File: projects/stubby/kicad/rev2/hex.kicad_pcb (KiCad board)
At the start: 2 copper layers, 49.5 x 49.5 mm, 62 parts, among them IC1 ATMEGA1284-A, P1 CONN_6, P10 PROG, P11 CONN_6, P2 CONN_6, P3 CONN_10, P4 CONN_13, P5 CONN_4, P6 CONN_2, P7 CONN_1, P8 CONN_4, P9 BATT (4.8V-6V), SW1 DPDT, X1 CRYSTAL_RESONATOR

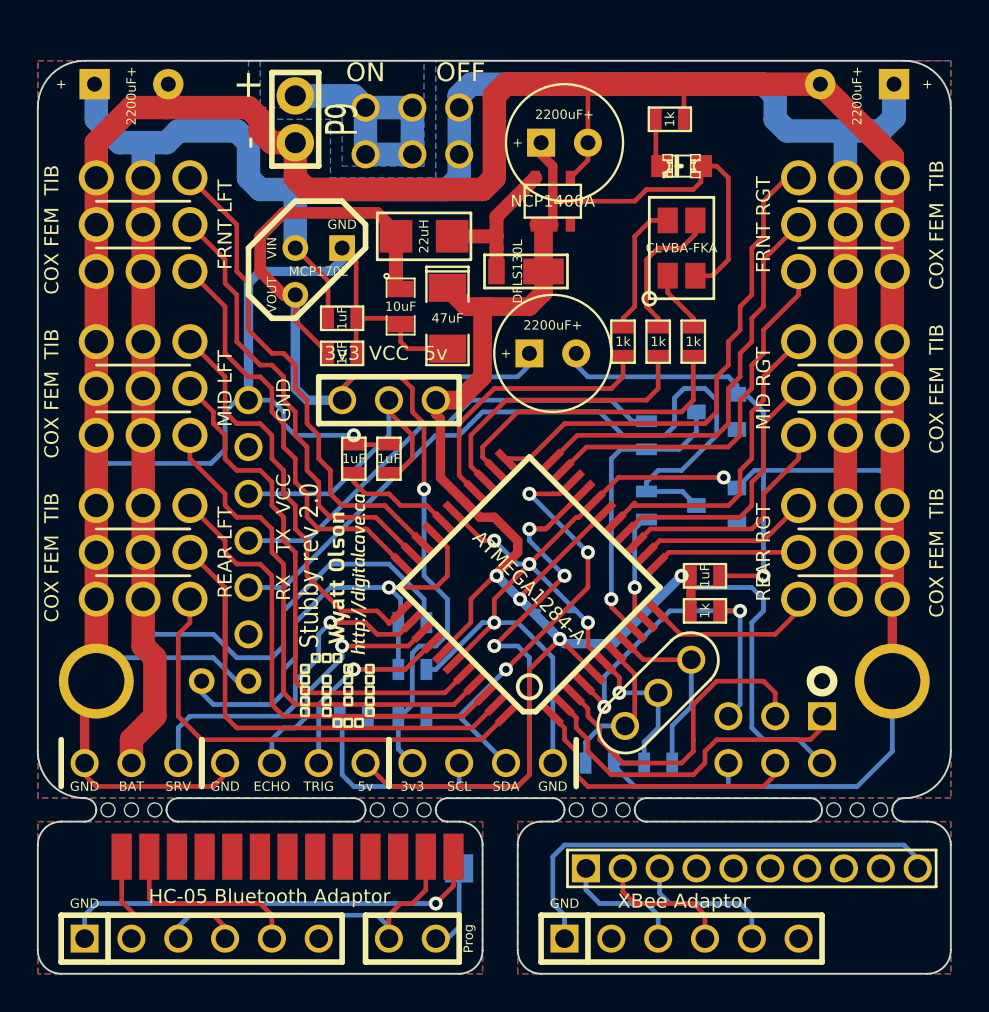
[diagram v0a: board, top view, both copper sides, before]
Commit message: A bit of trace cleanup
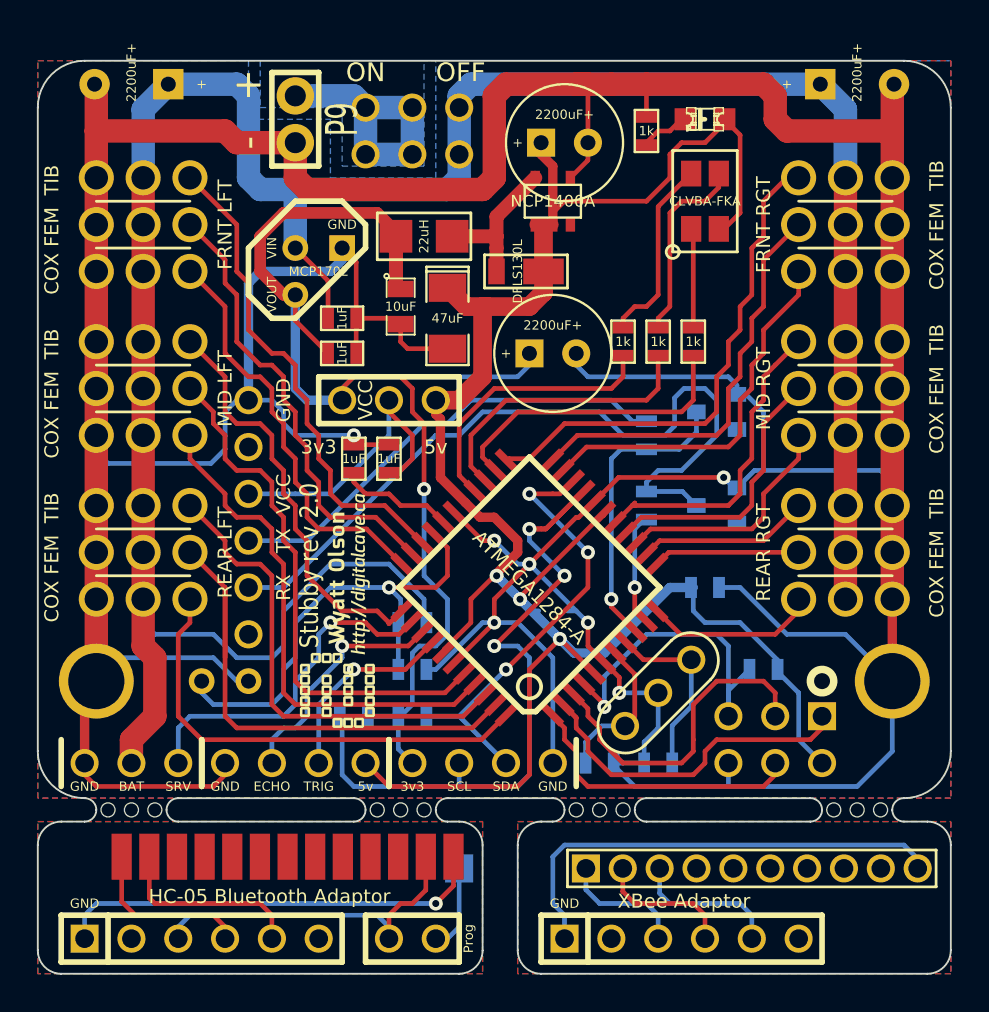
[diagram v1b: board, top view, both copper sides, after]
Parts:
- C10, R1: moved to B.Cu
- moved R1 4.49 mm to (74.9, 47.6), turned to 180 degrees
- moved D2 2.84 mm to (71.8, 17.8)
- moved D3 2.84 mm to (71.8, 22.2)
- moved R2 1.42 mm to (68.6, 18.4), turned to 90 degrees
- moved C10 0.63 mm to (71.8, 43.2)
- turned C13 to 0 degrees
- turned C14 to 180 degrees
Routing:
- net GND: track 304.8 -> 312.4 mm, vias 8 -> 7
- net +BATT: track 149.3 -> 144.9 mm
- net /LED_GR_R: track 7.36 -> 10.3 mm
- net +5V: track 118.1 -> 115.4 mm, vias 4 -> 3
- net /LED_BL_R: track 7.92 -> 10.5 mm
- net /LED_RD_R: track 3.39 -> 5.41 mm
- net /RESET: track 19.4 -> 18.2 mm, vias 2 -> 1

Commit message: Moved some more components to the front layer... now there are only four SMD components on the back (2x 100k for battery meter, and 2x 4.7k for I2C bus)
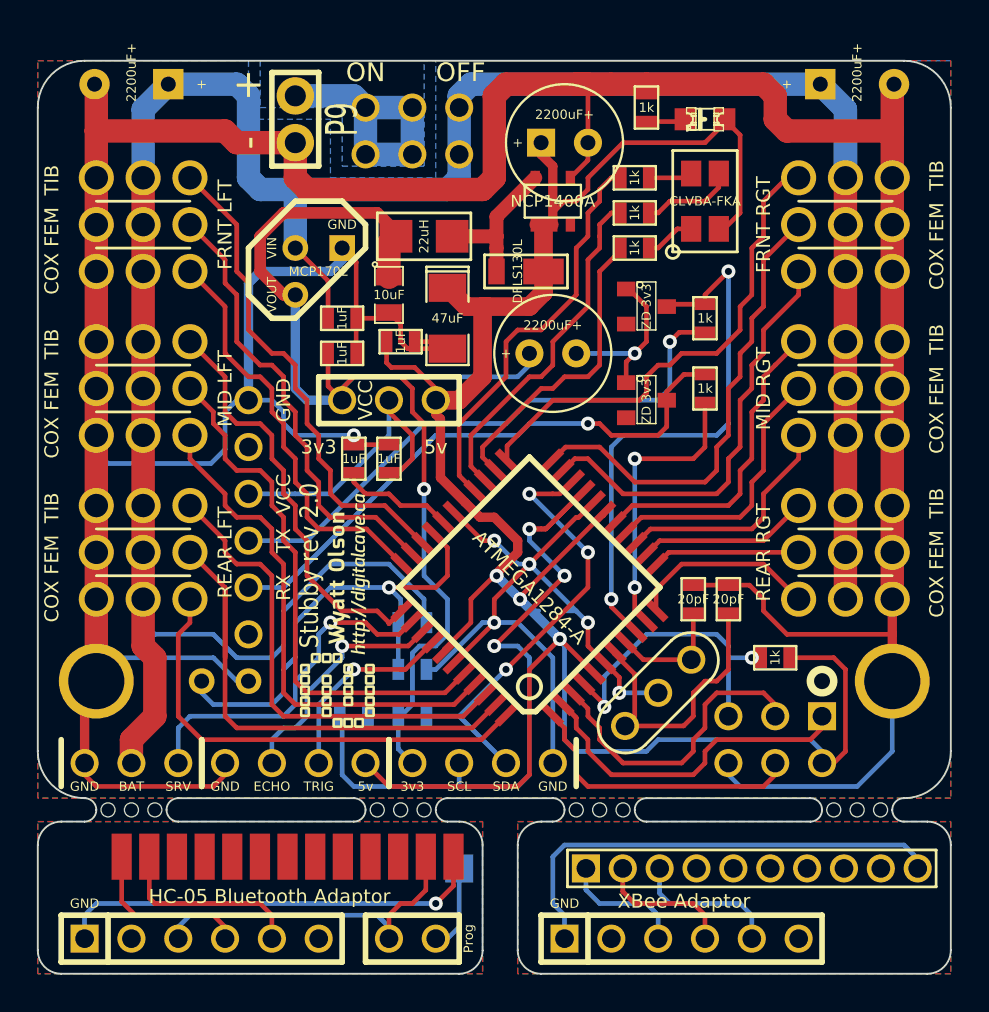
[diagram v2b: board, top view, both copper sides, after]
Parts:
- C10, C6, C7, R1, R7, R8, ZD1, ZD2: moved to F.Cu
- moved C10 21.2 mm to (55.2, 29.8)
- moved C6 11.3 mm to (73.0, 43.8), turned to 270 degrees
- moved C7 9.09 mm to (71.1, 43.8), turned to 270 degrees
- moved R9 8.91 mm to (67.9, 21.0), turned to 0 degrees
- moved R10 7.10 mm to (67.9, 22.9), turned to 0 degrees
- moved R7 7.10 mm to (71.8, 32.4)
- moved R8 7.10 mm to (71.8, 28.6), turned to 270 degrees
- moved ZD1 6.87 mm to (68.6, 27.9)
- moved ZD2 6.87 mm to (68.6, 33.0)
- moved R11 5.99 mm to (67.9, 24.8), turned to 0 degrees
- moved R2 1.27 mm to (68.6, 17.1)
- moved C1 0.90 mm to (54.6, 27.3)
- moved R1 0.90 mm to (75.6, 47.0)
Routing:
- net GND: track 312.4 -> 275.8 mm
- net /AVR_RX: track 16.2 -> 30.1 mm, vias 1 -> 2
- net +5V: track 115.4 -> 127.7 mm
- net N-0000012: track 42.4 -> 31.2 mm, vias 0 -> 1
- net /AVR_TX: track 6.09 -> 15.5 mm, vias 1 -> 2
- net /LED_GR_R: track 10.3 -> 2.39 mm
- net /XTAL2: track 8.36 -> 15.4 mm
- net /LED_GR: track 15.2 -> 22.1 mm
- net N-0000011: track 25.2 -> 30.9 mm, vias 0 -> 1
- net /LED_BL_R: track 10.5 -> 5.12 mm
- net /XTAL1: track 10.1 -> 6.59 mm
- net /LED_BL: track 15.9 -> 19.0 mm
- net /PWM04: track 22.8 -> 25.5 mm
- net /PWM05: track 20.7 -> 23.4 mm
- net /LED_RD_R: track 5.41 -> 2.73 mm
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
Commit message: Removed i2c resistors (they can be on whatever board you connect to Stubby); moved battery meter resistors to top of board.  All SMD components are now on top to make manufacturing easier / cheaper
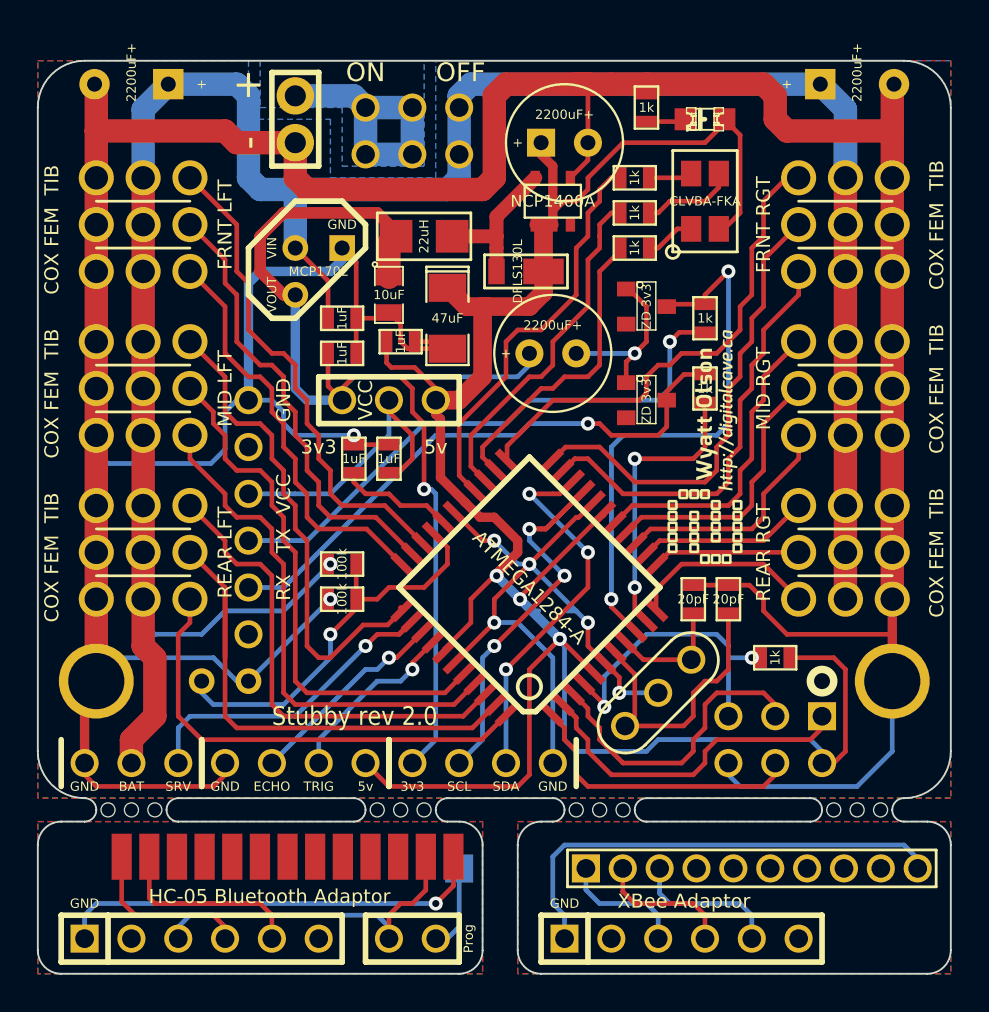
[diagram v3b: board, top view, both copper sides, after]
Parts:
- removed R3, R4: 4k7, SM0603_VALUE
- R5, R6: moved to F.Cu
- moved VAL 21.8 mm to (71.8, 35.6)
- moved R6 5.39 mm to (52.1, 43.8), turned to 0 degrees
- moved R5 4.96 mm to (52.1, 41.9), turned to 0 degrees
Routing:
- net /I2C_SCL: track 39.9 -> 23.3 mm
- net +BATT: track 144.9 -> 135.7 mm, vias 0 -> 1
- net /ADC_BATTERY_METER: track 26.3 -> 22.3 mm
- net /I2C_SDA: track 24.3 -> 20.4 mm
- net /PWM08: track 23.0 -> 26.7 mm
- net +3.3V: track 67.7 -> 64.5 mm
- net /DIST_ECHO: track 13.1 -> 11.2 mm
- net GND: track 275.8 -> 277.5 mm, vias 7 -> 8
- net /DIST_SERVO: track 19.1 -> 18.1 mm
- net /DIST_TRIG: track 10.9 -> 9.95 mm

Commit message: Changed battery meter capacitor to be SMD (so as to not be in the way of the radio).  Re-routed some traces to reduce via count.  All components (SMD + through hole) are now on the top of the board.
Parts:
- C11: footprint C1V5 -> SM1206POL; moved to F.Cu
- moved C10 27.1 mm to (76.2, 47.0), turned to 90 degrees
- moved R1 1.27 mm to (74.3, 47.0), turned to 270 degrees
- moved C1 1.20 mm to (55.0, 28.4)
- moved C11 0.90 mm to (45.1, 48.9), turned to 180 degrees
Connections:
- P5 pad 2: /I2C_SCL -> /I2C_SDA
- P5 pad 3: /I2C_SDA -> /I2C_SCL
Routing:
- net GND: track 277.5 -> 289.1 mm, vias 8 -> 9
- net +5V: track 127.7 -> 119.3 mm, vias 3 -> 4
- net /ADC_BATTERY_METER: track 22.3 -> 17.8 mm, vias 1 -> 2
- net /I2C_SDA: track 20.4 -> 22.5 mm, vias 3 -> 1
- net /AVR_RX: track 30.1 -> 31.9 mm
- net /SCK: track 16.8 -> 15.1 mm
- net /XTAL2: track 15.4 -> 14.3 mm
- net /PWM12: track 25.6 -> 26.6 mm
- net /MISO: track 19.5 -> 18.6 mm
- net /RESET: track 17.0 -> 16.1 mm
- net +3.3V: track 64.5 -> 65.3 mm
- net /PWM13: track 29.0 -> 29.6 mm
- net /I2C_SCL: track 23.3 -> 23.8 mm, vias 3 -> 1
- net /MOSI: track 15.8 -> 16.3 mm

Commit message: Cleaned up tracks
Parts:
- moved C9 1.27 mm to (64.1, 17.8)
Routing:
- net /PWM13: track 29.6 -> 25.8 mm
- net +3.3V: track 65.3 -> 62.0 mm
- net GND: track 289.1 -> 286.0 mm
- net +BATT: track 135.7 -> 133.1 mm
- net /PWM12: track 26.6 -> 24.7 mm
- net /AVR_RX: track 31.9 -> 30.1 mm
- net +5V: track 119.3 -> 120.4 mm
- net /MISO: track 18.6 -> 17.6 mm
- net /DIST_SERVO: track 18.1 -> 17.1 mm
- net /MOSI: track 16.3 -> 15.4 mm

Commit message: Re-annotated board
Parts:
- renumbered C2 to C1, C11 to C10, C6 to C11, C7 to C12, C5 to C13, C12 to C14, C3 to C2, C4 to C3, C13 to C4, C14 to C5, C1 to C6, C8 to C7, C9 to C8, C10 to C9, P9 to P1, P5 to P10, P8 to P11, P10 to P2, P1 to P4, P4 to P5, P11 to P6, P2 to P8, P6 to P9, R2 to R1, R5 to R2, R6 to R3, R1 to R4, R9 to R5, R10 to R6, R11 to R7, R7 to R8, R8 to R9, S2 to S1, S3 to S2, S4 to S3, S5 to S4, S6 to S5, S7 to S6, S1 to S7
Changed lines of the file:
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@@
   )
   (setup
-    (last_trace_width 0.508)
+    (last_trace_width 0.254)
     (user_trace_width 0.381)
     (user_trace_width 0.508)
@@
     (descr "Connecteurs 2 pins")
     (tags "CONN DEV")
-    (fp_text reference P9 (at 0 -2.54 270) (layer F.SilkS) hide
+    (fp_text reference P1 (at 0 -2.54 270) (layer F.SilkS) hide
       (effects (font (size 1.72974 1.08712) (thickness 0.27178)))
     )
@@
     (descr "Connecteur 4 pibs")
     (tags "CONN DEV")
-    (fp_text reference P5 (at 0 -2.54) (layer F.SilkS) hide
+    (fp_text reference P10 (at 0 -2.54) (layer F.SilkS) hide
       (effects (font (size 1.73482 1.08712) (thickness 0.27178)))
     )
@@
     (descr "Connecteur 4 pibs")
     (tags "CONN DEV")
-    (fp_text reference P8 (at 0 -2.54 180) (layer F.SilkS) hide
+    (fp_text reference P11 (at 0 -2.54 180) (layer F.SilkS) hide
       (effects (font (size 1.73482 1.08712) (thickness 0.27178)))
     )
@@
     (descr "Connecteur 3 pins")
     (tags "CONN DEV")
-    (fp_text reference S1 (at 0 -2.54) (layer F.SilkS) hide
+    (fp_text reference S7 (at 0 -2.54) (layer F.SilkS) hide
       (effects (font (size 1.7907 1.07696) (thickness 0.26924)))
     )
@@
   (module C1V8 (layer F.Cu)
     (at 40.64 15.875 180)
-    (fp_text reference C14 (at 0 2.032 180) (layer F.SilkS) hide
+    (fp_text reference C5 (at 0 2.032 180) (layer F.SilkS) hide
       (effects (font (size 1.016 0.889) (thickness 0.2032)))
     )
@@
     (descr "Connecteur 6 pins")
     (tags "CONN DEV")
-    (fp_text reference P11 (at 0 -2.54 270) (layer F.SilkS) hide
+    (fp_text reference P6 (at 0 -2.54 270) (layer F.SilkS) hide
       (effects (font (size 1.72974 1.08712) (thickness 0.27178)))
     )
@@
   (module C1V8 (layer F.Cu)
     (at 80.01 15.875)
-    (fp_text reference C13 (at 0 2.032) (layer F.SilkS) hide
+    (fp_text reference C4 (at 0 2.032) (layer F.SilkS) hide
       (effects (font (size 1.016 0.889) (thickness 0.2032)))
     )
@@
     (descr "Connecteur 6 pins")
     (tags "CONN DEV")
-    (fp_text reference P1 (at 0 -2.54) (layer F.SilkS) hide
+    (fp_text reference P4 (at 0 -2.54) (layer F.SilkS) hide
       (effects (font (size 1.72974 1.08712) (thickness 0.27178)))
     )
@@
     (descr "Connecteurs 2 pins")
     (tags "CONN DEV")
-    (fp_text reference P6 (at 0 -2.54 180) (layer F.SilkS) hide
+    (fp_text reference P9 (at 0 -2.54 180) (layer F.SilkS) hide
       (effects (font (size 1.72974 1.08712) (thickness 0.27178)))
     )
@@
     (descr "Connecteur 6 pins")
     (tags "CONN DEV")
-    (fp_text reference P2 (at 0 -2.54) (layer F.SilkS) hide
+    (fp_text reference P8 (at 0 -2.54) (layer F.SilkS) hide
       (effects (font (size 1.72974 1.08712) (thickness 0.27178)))
     )
@@
   (module HEX_LEG (layer F.Cu)
     (at 41.91 30.48 180)
-    (fp_text reference S4 (at -7.112 -1.524 270) (layer F.SilkS) hide
+    (fp_text reference S3 (at -7.112 -1.524 270) (layer F.SilkS) hide
       (effects (font (size 1 1) (thickness 0.15)))
     )
@@
   (module HEX_LEG (layer F.Cu)
     (at 41.91 21.59 180)
-    (fp_text reference S2 (at -7.112 -1.524 270) (layer F.SilkS) hide
+    (fp_text reference S1 (at -7.112 -1.524 270) (layer F.SilkS) hide
       (effects (font (size 1 1) (thickness 0.15)))
     )
@@
   (module HEX_LEG (layer F.Cu)
     (at 41.91 39.37 180)
-    (fp_text reference S6 (at -7.112 -1.524 270) (layer F.SilkS) hide
+    (fp_text reference S5 (at -7.112 -1.524 270) (layer F.SilkS) hide
       (effects (font (size 1 1) (thickness 0.15)))
     )
@@
   (module HEX_LEG_REVERSE (layer F.Cu)
     (at 78.74 25.4)
-    (fp_text reference S3 (at -8 -3 90) (layer F.SilkS) hide
+    (fp_text reference S2 (at -8 -3 90) (layer F.SilkS) hide
       (effects (font (size 1 1) (thickness 0.15)))
     )
@@
   (module HEX_LEG_REVERSE (layer F.Cu)
     (at 78.74 34.29)
-    (fp_text reference S5 (at -8 -3 90) (layer F.SilkS) hide
+    (fp_text reference S4 (at -8 -3 90) (layer F.SilkS) hide
       (effects (font (size 1 1) (thickness 0.15)))
     )
@@
   (module HEX_LEG_REVERSE (layer F.Cu)
     (at 78.74 43.18)
-    (fp_text reference S7 (at -8 -3 90) (layer F.SilkS) hide
+    (fp_text reference S6 (at -8 -3 90) (layer F.SilkS) hide
       (effects (font (size 1 1) (thickness 0.15)))
     )
@@
     (descr "ISP Header")
     (tags ISP)
-    (fp_text reference P10 (at 0 -3.81 180) (layer F.SilkS) hide
+    (fp_text reference P2 (at 0 -3.81 180) (layer F.SilkS) hide
       (effects (font (size 1.016 1.016) (thickness 0.2032)))
     )
@@
     (at 54.61 57.785)
     (tags "Bluetooth HC05 HC06")
-    (fp_text reference P4 (at -10.16 -2.54) (layer F.SilkS) hide
+    (fp_text reference P5 (at -10.16 -2.54) (layer F.SilkS) hide
       (effects (font (size 1.72974 1.08712) (thickness 0.27178)))
     )
@@
     (at 71.755 28.575 270)
     (attr smd)
-    (fp_text reference R8 (at 0 0 270) (layer F.SilkS) hide
+    (fp_text reference R9 (at 0 0 270) (layer F.SilkS) hide
       (effects (font (size 0.508 0.508) (thickness 0.1143)))
     )
@@
     (at 68.58 17.145 90)
     (attr smd)
-    (fp_text reference R2 (at 0 0 90) (layer F.SilkS) hide
+    (fp_text reference R1 (at 0 0 90) (layer F.SilkS) hide
       (effects (font (size 0.508 0.508) (thickness 0.1143)))
     )
@@
     (at 73.025 43.815 270)
     (attr smd)
-    (fp_text reference C6 (at 0 0 270) (layer F.SilkS) hide
+    (fp_text reference C11 (at 0 0 270) (layer F.SilkS) hide
       (effects (font (size 0.508 0.508) (thickness 0.1143)))
     )
@@
     (at 71.12 43.815 270)
     (attr smd)
-    (fp_text reference C7 (at 0 0 270) (layer F.SilkS) hide
+    (fp_text reference C12 (at 0 0 270) (layer F.SilkS) hide
       (effects (font (size 0.508 0.508) (thickness 0.1143)))
     )
@@
     (at 71.755 32.385 90)
     (attr smd)
-    (fp_text reference R7 (at 0 0 90) (layer F.SilkS) hide
+    (fp_text reference R8 (at 0 0 90) (layer F.SilkS) hide
       (effects (font (size 0.508 0.508) (thickness 0.1143)))
     )
@@
     (at 74.295 46.99 270)
     (attr smd)
-    (fp_text reference R1 (at 0 0 270) (layer F.SilkS) hide
+    (fp_text reference R4 (at 0 0 270) (layer F.SilkS) hide
       (effects (font (size 0.508 0.508) (thickness 0.1143)))
     )
@@
     (at 52.705 36.195 270)
     (attr smd)
-    (fp_text reference C5 (at 0 0 270) (layer F.SilkS) hide
+    (fp_text reference C13 (at 0 0 270) (layer F.SilkS) hide
       (effects (font (size 0.508 0.508) (thickness 0.1143)))
     )
@@
     (at 52.07 28.575)
     (attr smd)
-    (fp_text reference C4 (at 0 0) (layer F.SilkS) hide
+    (fp_text reference C3 (at 0 0) (layer F.SilkS) hide
       (effects (font (size 0.508 0.508) (thickness 0.1143)))
     )
@@
     (at 52.07 30.48)
     (attr smd)
-    (fp_text reference C3 (at 0 0) (layer F.SilkS) hide
+    (fp_text reference C2 (at 0 0) (layer F.SilkS) hide
       (effects (font (size 0.508 0.508) (thickness 0.1143)))
     )
@@
     (at 52.07 41.91)
     (attr smd)
-    (fp_text reference R5 (at 0 0) (layer F.SilkS) hide
+    (fp_text reference R2 (at 0 0) (layer F.SilkS) hide
       (effects (font (size 0.508 0.508) (thickness 0.1143)))
     )
@@
     (at 52.07 43.815)
     (attr smd)
-    (fp_text reference R6 (at 0 0) (layer F.SilkS) hide
+    (fp_text reference R3 (at 0 0) (layer F.SilkS) hide
       (effects (font (size 0.508 0.508) (thickness 0.1143)))
     )
@@
     (at 67.945 20.955)
     (attr smd)
-    (fp_text reference R9 (at 0 0) (layer F.SilkS) hide
+    (fp_text reference R5 (at 0 0) (layer F.SilkS) hide
       (effects (font (size 0.508 0.508) (thickness 0.1143)))
     )
@@
     (at 67.945 24.765)
     (attr smd)
-    (fp_text reference R11 (at 0 0) (layer F.SilkS) hide
+    (fp_text reference R7 (at 0 0) (layer F.SilkS) hide
       (effects (font (size 0.508 0.508) (thickness 0.1143)))
     )
@@
     (at 67.945 22.86)
     (attr smd)
-    (fp_text reference R10 (at 0 0) (layer F.SilkS) hide
+    (fp_text reference R6 (at 0 0) (layer F.SilkS) hide
       (effects (font (size 0.508 0.508) (thickness 0.1143)))
     )
@@
     (at 57.785 28.575 270)
     (attr smd)
-    (fp_text reference C8 (at 0 0 270) (layer F.SilkS) hide
+    (fp_text reference C7 (at 0 0 270) (layer F.SilkS) hide
       (effects (font (size 0.762 0.762) (thickness 0.127)))
     )
@@
   (module C1V7 (layer F.Cu)
     (at 63.5 30.48)
-    (fp_text reference C2 (at 0 1.524) (layer F.SilkS) hide
+    (fp_text reference C1 (at 0 1.524) (layer F.SilkS) hide
       (effects (font (size 1.143 0.889) (thickness 0.2032)))
     )
@@
     (at 54.991 28.448 270)
     (attr smd)
-    (fp_text reference C1 (at 0 -0.3175 270) (layer F.SilkS) hide
+    (fp_text reference C6 (at 0 -0.3175 270) (layer F.SilkS) hide
       (effects (font (size 0.50038 0.50038) (thickness 0.10922)))
     )
@@
   (module C1V7 (layer F.Cu)
     (at 64.135 17.78)
-    (fp_text reference C9 (at 0 1.524) (layer F.SilkS) hide
+    (fp_text reference C8 (at 0 1.524) (layer F.SilkS) hide
       (effects (font (size 1.143 0.889) (thickness 0.2032)))
     )
@@
     (at 76.2 46.99 90)
     (attr smd)
-    (fp_text reference C10 (at 0 0 90) (layer F.SilkS) hide
+    (fp_text reference C9 (at 0 0 90) (layer F.SilkS) hide
       (effects (font (size 0.508 0.508) (thickness 0.1143)))
     )
@@
     (at 54.61 36.195 270)
     (attr smd)
-    (fp_text reference C12 (at 0 0 270) (layer F.SilkS) hide
+    (fp_text reference C14 (at 0 0 270) (layer F.SilkS) hide
       (effects (font (size 0.508 0.508) (thickness 0.1143)))
     )
@@
     (at 45.085 48.895 180)
     (attr smd)
-    (fp_text reference C11 (at 0 0 180) (layer F.SilkS) hide
+    (fp_text reference C10 (at 0 0 180) (layer F.SilkS) hide
       (effects (font (size 0.762 0.762) (thickness 0.127)))
     )
